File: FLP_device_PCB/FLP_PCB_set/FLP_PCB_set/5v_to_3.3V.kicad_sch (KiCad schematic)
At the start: 8 parts, among them Q3 DMG3415UQ-7, U10 AP2112K-3.3

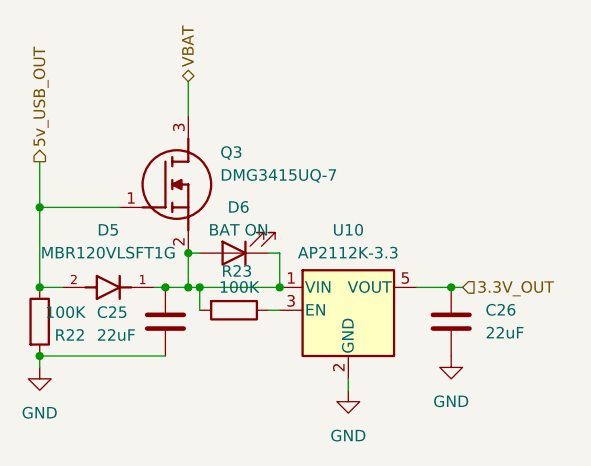
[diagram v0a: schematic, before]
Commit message: PCB fixing end adding description pdf
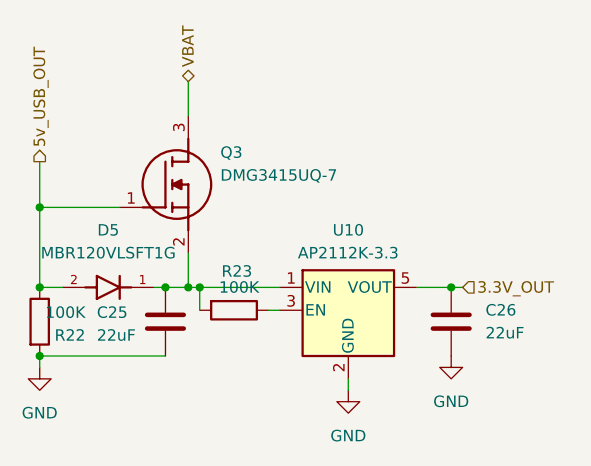
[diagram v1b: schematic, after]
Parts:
- removed D6: BAT ON, LED_SMD:LED_0805_2012Metric, symbol Device:LED
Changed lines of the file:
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@@
-	)
-	(junction
-		(at 45.72 41.91)
-		(diameter 0)
-		(color 0 0 0 0)
 	)
 	(junction
@@
 	)
 	(junction
-		(at 55.88 45.72)
-		(diameter 0)
-		(color 0 0 0 0)
-	)
-	(junction
 		(at 45.72 45.72)
 		(diameter 0)
@@
 	(wire
 		(pts
-			(xy 55.88 41.91) (xy 54.61 41.91)
-		)
-		(stroke
-			(width 0)
-			(type default)
-		)
-	)
-	(wire
-		(pts
-			(xy 46.99 41.91) (xy 45.72 41.91)
-		)
-		(stroke
-			(width 0)
-			(type default)
-		)
-	)
-	(wire
-		(pts
 			(xy 74.93 45.72) (xy 76.2 45.72)
 		)
@@
 		(pts
 			(xy 29.21 53.34) (xy 43.18 53.34)
-		)
-		(stroke
-			(width 0)
-			(type default)
-		)
-	)
-	(wire
-		(pts
-			(xy 55.88 41.91) (xy 55.88 45.72)
 		)
 		(stroke
@@
 					(unit 1)
 				)
-			)
-		)
-	)
-	(symbol
-		(lib_id "Device:LED")
-		(at 50.8 41.91 180)
-		(unit 1)
-		(exclude_from_sim no)
-		(in_bom yes)
-		(on_board yes)
-		(dnp no)
-		(property "Reference" "D6"
-			(at 51.308 36.83 0)
-			(effects
-				(font
-					(size 1.27 1.27)
-				)
-			)
-		)
-		(property "Value" "BAT ON"
-			(at 51.308 39.37 0)
-			(effects
-				(font
-					(size 1.27 1.27)
-				)
-			)
-		)
-		(property "Footprint" "LED_SMD:LED_0805_2012Metric"
-			(at 50.8 41.91 0)
-			(effects
-				(font
-					(size 1.27 1.27)
-				)
-				(hide yes)
-			)
-		)
-		(property "Datasheet" "~"
-			(at 50.8 41.91 0)
-			(effects
-				(font
-					(size 1.27 1.27)
-				)
-				(hide yes)
-			)
-		)
-		(property "Description" "Light emitting diode"
-			(at 50.8 41.91 0)
-			(effects
-				(font
-					(size 1.27 1.27)
-				)
-				(hide yes)
-			)
-		)
-		(property "Sim.Pins" "1=K 2=A"
-			(at 50.8 41.91 0)
-			(effects
-				(font
-					(size 1.27 1.27)
-				)
-				(hide yes)
-			)
-		)
-		(pin "1"
-		)
-		(pin "2"
-		)
-		(instances
-			(project "FLP_PCB_set"
-				(path "/3f8c5218-62bd-4afc-a38b-629e4a961e52/cb21122d-83f9-4f10-9012-eb16f816aa97/ada91f11-1394-4bbf-b7f9-c4d19c7b4248"
-					(reference "D6")
-					(unit 1)
-				)
